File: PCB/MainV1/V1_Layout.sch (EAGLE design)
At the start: 47 parts, among them IC1 LM6482, IC2 AD623N, U2 MB85RC256VPF-G-JNERE2

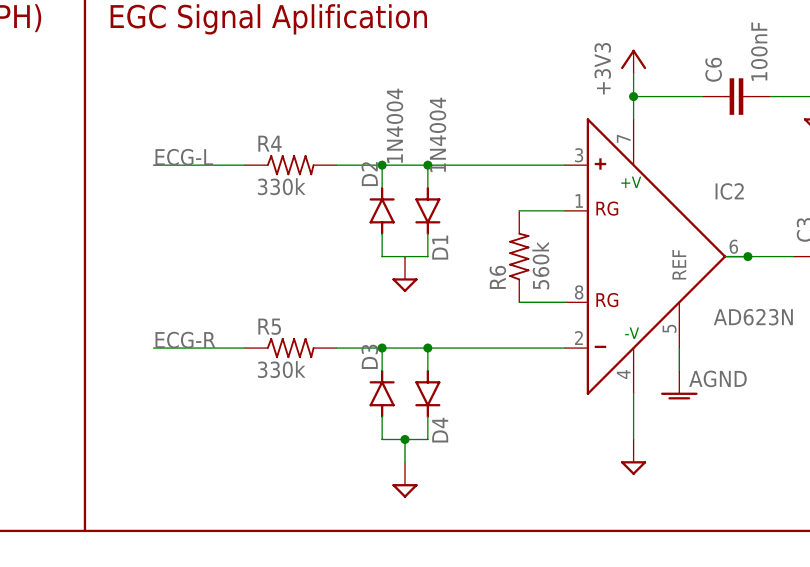
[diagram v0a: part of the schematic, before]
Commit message: Reviewed layout, added text, rounded corners. Design rule check passed. Ready for final review
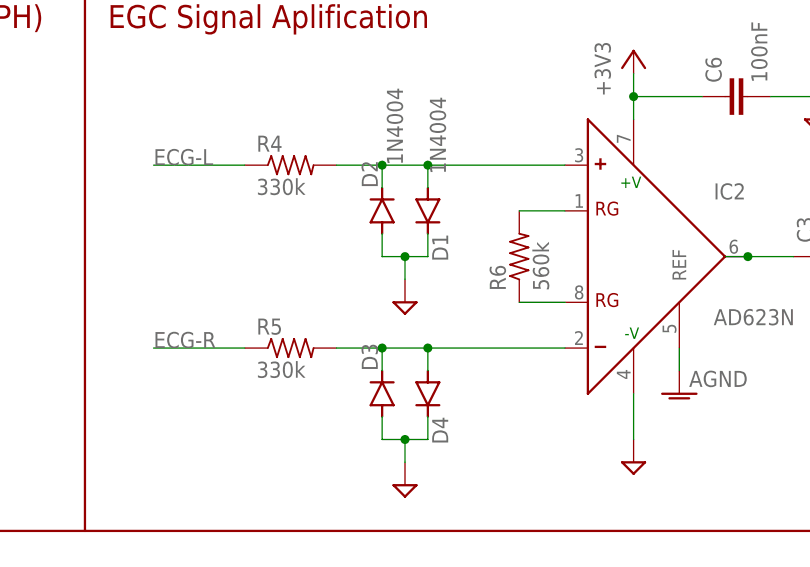
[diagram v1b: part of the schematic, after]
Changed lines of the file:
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@@
 <attribute name="NAME" x="264.6426" y="68.58" size="1.778" layer="95" rot="R270"/>
 </instance>
-<instance part="SUPPLY1" gate="GND" x="261.62" y="83.82" smashed="yes"/>
+<instance part="SUPPLY1" gate="GND" x="261.62" y="81.28" smashed="yes"/>
 <instance part="SUPPLY2" gate="GND" x="261.62" y="60.96" smashed="yes"/>
 <instance part="U2" gate="G$1" x="50.8" y="68.58" smashed="yes"/>
@@
 <wire x1="261.62" y1="66.04" x2="261.62" y2="63.5" width="0.1524" layer="91"/>
 <pinref part="SUPPLY2" gate="GND" pin="GND"/>
-</segment>
-<segment>
-<pinref part="D2" gate="1" pin="A"/>
-<wire x1="259.08" y1="88.9" x2="259.08" y2="86.36" width="0.1524" layer="91"/>
-<wire x1="261.62" y1="86.36" x2="264.16" y2="86.36" width="0.1524" layer="91"/>
-<pinref part="D1" gate="1" pin="C"/>
-<wire x1="264.16" y1="86.36" x2="264.16" y2="88.9" width="0.1524" layer="91"/>
-<wire x1="259.08" y1="86.36" x2="261.62" y2="86.36" width="0.1524" layer="91"/>
-<pinref part="SUPPLY1" gate="GND" pin="GND"/>
 </segment>
 <segment>
@@
 <wire x1="73.66" y1="15.24" x2="73.66" y2="12.7" width="0.1524" layer="91"/>
 </segment>
+<segment>
+<pinref part="D2" gate="1" pin="A"/>
+<wire x1="259.08" y1="88.9" x2="259.08" y2="86.36" width="0.1524" layer="91"/>
+<pinref part="D1" gate="1" pin="C"/>
+<wire x1="264.16" y1="86.36" x2="264.16" y2="88.9" width="0.1524" layer="91"/>
+<wire x1="259.08" y1="86.36" x2="261.62" y2="86.36" width="0.1524" layer="91"/>
+<pinref part="SUPPLY1" gate="GND" pin="GND"/>
+<wire x1="261.62" y1="86.36" x2="264.16" y2="86.36" width="0.1524" layer="91"/>
+<wire x1="261.62" y1="83.82" x2="261.62" y2="86.36" width="0.1524" layer="91"/>
+<junction x="261.62" y="86.36"/>
+</segment>
 </net>
 <net name="N$2" class="0">
@@
 </sheet>
 </sheets>
+<errors>
+</errors>
 </schematic>
 </drawing>

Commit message: Ordered. Added CAM files. Added 3D desgn files for Fusion 360.
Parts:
- added C7: 1uF, rcl:C-EUC0603
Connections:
- net +3V3: now also C7.1
- net GND: now also C7.2
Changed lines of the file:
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@@
 <part name="ACCEL2" library="con-molex" library_urn="urn:adsk.eagle:library:165" deviceset="22-?-05" device="05-7058"/>
 <part name="C10" library="rcl" library_urn="urn:adsk.eagle:library:334" deviceset="CPOL-EU" device="TAP5-45" package3d_urn="urn:adsk.eagle:package:23333/3" value="10uF"/>
+<part name="C7" library="rcl" library_urn="urn:adsk.eagle:library:334" deviceset="C-EU" device="C0603" package3d_urn="urn:adsk.eagle:package:23616/2" value="1uF"/>
 </parts>
 <sheets>
@@
 <attribute name="VALUE" x="140.843" y="23.3426" size="1.778" layer="96"/>
 </instance>
+<instance part="C7" gate="G$1" x="73.66" y="81.28" smashed="yes">
+<attribute name="NAME" x="75.184" y="81.661" size="1.778" layer="95"/>
+<attribute name="VALUE" x="75.184" y="76.581" size="1.778" layer="96"/>
+</instance>
 </instances>
 <busses>
@@
 <pinref part="SUPPLY7" gate="GND" pin="GND"/>
 <wire x1="73.66" y1="71.12" x2="71.12" y2="71.12" width="0.1524" layer="91"/>
+<pinref part="C7" gate="G$1" pin="2"/>
+<wire x1="73.66" y1="76.2" x2="73.66" y2="71.12" width="0.1524" layer="91"/>
+<junction x="73.66" y="71.12"/>
 </segment>
 <segment>
@@
 <wire x1="71.12" y1="86.36" x2="73.66" y2="86.36" width="0.1524" layer="91"/>
 <wire x1="73.66" y1="86.36" x2="73.66" y2="88.9" width="0.1524" layer="91"/>
-</segment>
-<segment>
+<pinref part="C7" gate="G$1" pin="1"/>
+<wire x1="73.66" y1="86.36" x2="73.66" y2="83.82" width="0.1524" layer="91"/>
+<junction x="73.66" y="86.36"/>
+</segment>
+<segment>

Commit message: Added comments in schematc
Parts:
- R3: value 330k -> 0R
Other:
- note added: "V1 Notes:"
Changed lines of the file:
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@@
 <part name="+3V8" library="supply1" library_urn="urn:adsk.eagle:library:371" deviceset="+3V3" device=""/>
 <part name="SUPPLY13" library="supply2" library_urn="urn:adsk.eagle:library:372" deviceset="GND" device=""/>
-<part name="R3" library="rcl" library_urn="urn:adsk.eagle:library:334" deviceset="R-US_" device="R0603" package3d_urn="urn:adsk.eagle:package:23555/2" value="330k"/>
+<part name="R3" library="rcl" library_urn="urn:adsk.eagle:library:334" deviceset="R-US_" device="R0603" package3d_urn="urn:adsk.eagle:package:23555/2" value="0R"/>
 <part name="SUPPLY14" library="supply2" library_urn="urn:adsk.eagle:library:372" deviceset="GND" device=""/>
 <part name="AGND1" library="supply1" library_urn="urn:adsk.eagle:library:371" deviceset="AGND" device=""/>
@@
 <text x="91.44" y="106.68" size="1.778" layer="97">Address: 0x1D and 0x1C</text>
 <text x="170.18" y="106.68" size="1.778" layer="97">Address: 0x90</text>
+<wire x1="167.64" y1="-2.54" x2="342.9" y2="-2.54" width="0.254" layer="94"/>
+<wire x1="342.9" y1="-2.54" x2="342.9" y2="55.88" width="0.254" layer="94"/>
+<text x="172.72" y="50.8" size="2.54" layer="94">V1 Notes:</text>
 </plain>
 <instances>
